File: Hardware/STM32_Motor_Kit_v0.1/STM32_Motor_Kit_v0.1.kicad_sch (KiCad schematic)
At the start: 13 parts

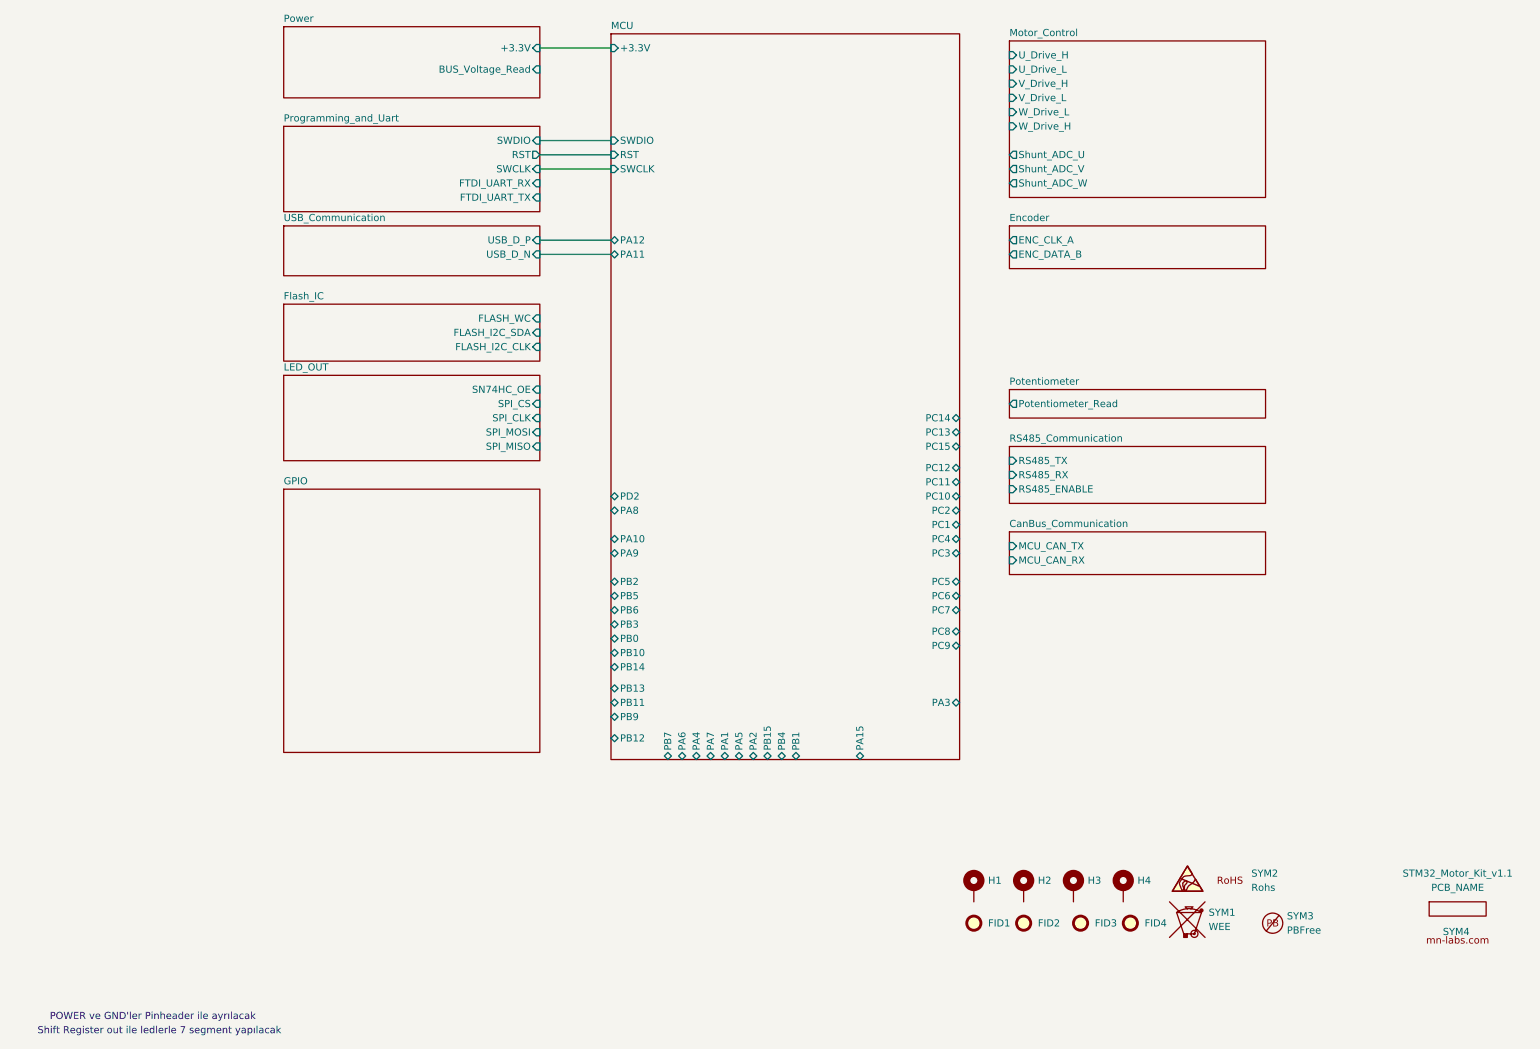
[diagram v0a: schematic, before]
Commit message: Firmware Configuration added, Motor Control Pins and BackEMF Analog Pins setted.
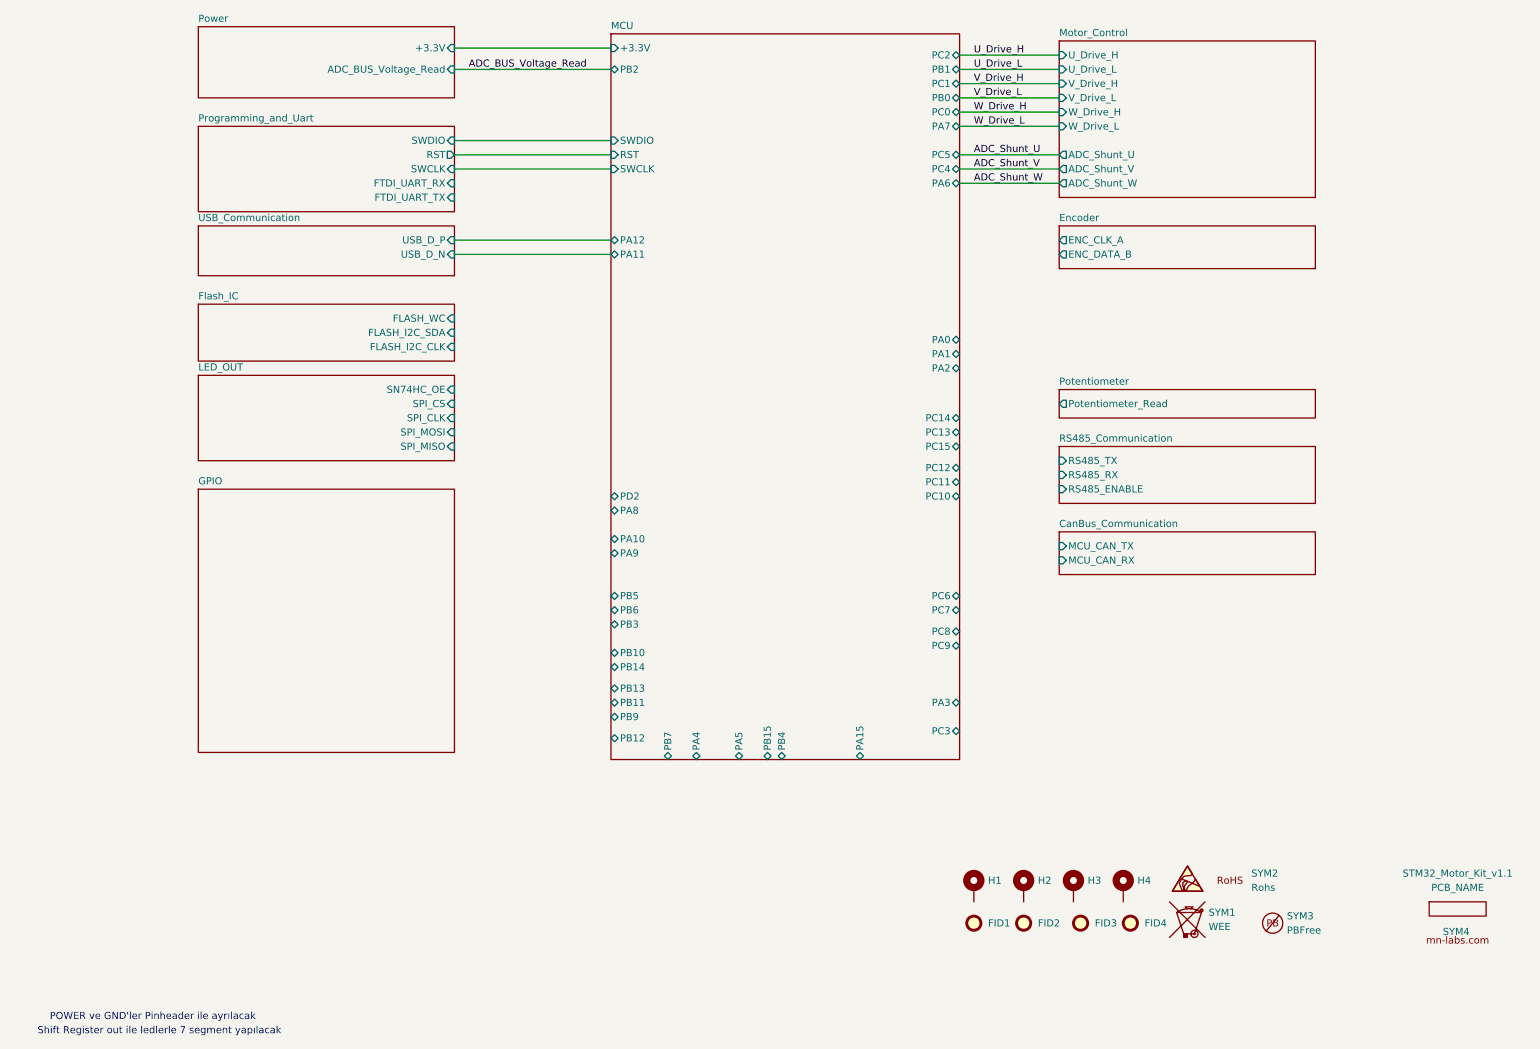
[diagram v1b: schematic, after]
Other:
- sheet MCU ports: added PA0, PC0; removed none
- sheet Motor_Control ports: added ADC_Shunt_U, ADC_Shunt_V, ADC_Shunt_W; removed Shunt_ADC_U, Shunt_ADC_V, Shunt_ADC_W
- sheet Power ports: added ADC_BUS_Voltage_Read; removed BUS_Voltage_Read

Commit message: 22.08.2024
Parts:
- added R104, R105, R106, R107, R108, R109, R110, R111, R112, R113, R114, R115, R116, R85, R86: 33R, AKE_Resistor_SMD:RES_0603, symbol AKE_Resistor:Resistor_US
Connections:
- net MCU/PA0: now also R111.1
- net MCU/PA1: now also R112.1
- net MCU/PA4: now also R110.1
- net MCU/PA5: now also R109.1
- net MCU/PB11: now also R113.1
- net MCU/PB12: now also R105.1
- net MCU/PB13: now also R85.1
- net MCU/PB14: now also R86.1
- net MCU/PB15: now also R104.1
- net MCU/PC10: now also R107.1
- net MCU/PC11: now also R106.1
- net MCU/PC12: now also R108.1
- net MCU/PC14: now also R115.1
- net MCU/PC15: now also R116.1
- net MCU/PC6: now also R114.1
- new net GPIO/Pin_1: R85.2
- new net GPIO/Pin_10: R111.2
- new net GPIO/Pin_11: R112.2
- new net GPIO/Pin_12: R113.2
- new net GPIO/Pin_13: R114.2
- new net GPIO/Pin_14: R115.2
- new net GPIO/Pin_15: R116.2
- new net GPIO/Pin_2: R86.2
- new net GPIO/Pin_3: R104.2
- new net GPIO/Pin_4: R105.2
- new net GPIO/Pin_5: R106.2
- new net GPIO/Pin_6: R107.2
- new net GPIO/Pin_7: R108.2
- new net GPIO/Pin_8: R109.2
- new net GPIO/Pin_9: R110.2
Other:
- added sheet User_Command (User_Command.kicad_sch)
- sheet GPIO ports: added Pin_1, Pin_10, Pin_11, Pin_12, Pin_13, Pin_14, Pin_15, Pin_2, Pin_3, Pin_4, Pin_5, Pin_6, Pin_7, Pin_8, Pin_9; removed none
- sheet MCU ports: added PB8; removed none

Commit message: 23.08.2024
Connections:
- net GPIO/Pin_1: now also R108.2; no longer R85.2
- net GPIO/Pin_10: now also R114.2; no longer R111.2
- net GPIO/Pin_11: now also R105.2; no longer R112.2
- net GPIO/Pin_13: now also R104.2; no longer R114.2
- net GPIO/Pin_14: now also R86.2; no longer R115.2
- net GPIO/Pin_15: now also R85.2; no longer R116.2
- net GPIO/Pin_2: now also R106.2; no longer R86.2
- net GPIO/Pin_3: now also R107.2; no longer R104.2
- net GPIO/Pin_4: now also R115.2; no longer R105.2
- net GPIO/Pin_5: now also R116.2; no longer R106.2
- net GPIO/Pin_6: now also R111.2; no longer R107.2
- net GPIO/Pin_7: now also R112.2; no longer R108.2
- net GPIO/Pin_8: now also R110.2; no longer R109.2
- net GPIO/Pin_9: now also R109.2; no longer R110.2
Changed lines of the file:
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@@
 		)
 		(pin "Pin_10" input
-			(at 87.63 127 0)
+			(at 87.63 134.62 0)
 			(effects
 				(font
@@
 		)
 		(pin "Pin_14" input
-			(at 87.63 137.16 0)
+			(at 87.63 104.14 0)
 			(effects
 				(font
@@
 		)
 		(pin "Pin_1" input
+			(at 87.63 118.11 0)
+			(effects
+				(font
+					(size 1.27 1.27)
+				)
+				(justify right)
+			)
+		)
+		(pin "Pin_3" input
+			(at 87.63 115.57 0)
+			(effects
+				(font
+					(size 1.27 1.27)
+				)
+				(justify right)
+			)
+		)
+		(pin "Pin_5" input
+			(at 87.63 139.7 0)
+			(effects
+				(font
+					(size 1.27 1.27)
+				)
+				(justify right)
+			)
+		)
+		(pin "Pin_7" input
+			(at 87.63 129.54 0)
+			(effects
+				(font
+					(size 1.27 1.27)
+				)
+				(justify right)
+			)
+		)
+		(pin "Pin_13" input
+			(at 87.63 106.68 0)
+			(effects
+				(font
+					(size 1.27 1.27)
+				)
+				(justify right)
+			)
+		)
+		(pin "Pin_15" input
 			(at 87.63 101.6 0)
 			(effects
@@
 			)
 		)
-		(pin "Pin_3" input
-			(at 87.63 106.68 0)
+		(pin "Pin_9" input
+			(at 87.63 121.92 0)
 			(effects
 				(font
@@
 			)
 		)
-		(pin "Pin_5" input
+		(pin "Pin_11" input
+			(at 87.63 109.22 0)
+			(effects
+				(font
+					(size 1.27 1.27)
+				)
+				(justify right)
+			)
+		)
+		(pin "Pin_8" input
+			(at 87.63 124.46 0)
+			(effects
+				(font
+					(size 1.27 1.27)
+				)
+				(justify right)
+			)
+		)
+		(pin "Pin_4" input
+			(at 87.63 137.16 0)
+			(effects
+				(font
+					(size 1.27 1.27)
+				)
+				(justify right)
+			)
+		)
+		(pin "Pin_2" input
 			(at 87.63 113.03 0)
 			(effects
@@
 			)
 		)
-		(pin "Pin_7" input
-			(at 87.63 118.11 0)
+		(pin "Pin_6" input
+			(at 87.63 127 0)
 			(effects
 				(font
-					(size 1.27 1.27)
-				)
-				(justify right)
-			)
-		)
-		(pin "Pin_13" input
-			(at 87.63 134.62 0)
-			(effects
-				(font
-					(size 1.27 1.27)
-				)
-				(justify right)
-			)
-		)
-		(pin "Pin_15" input
-			(at 87.63 139.7 0)
-			(effects
-				(font
-					(size 1.27 1.27)
-				)
-				(justify right)
-			)
-		)
-		(pin "Pin_9" input
-			(at 87.63 124.46 0)
-			(effects
-				(font
-					(size 1.27 1.27)
-				)
-				(justify right)
-			)
-		)
-		(pin "Pin_11" input
-			(at 87.63 129.54 0)
-			(effects
-				(font
-					(size 1.27 1.27)
-				)
-				(justify right)
-			)
-		)
-		(pin "Pin_8" input
-			(at 87.63 121.92 0)
-			(effects
-				(font
-					(size 1.27 1.27)
-				)
-				(justify right)
-			)
-		)
-		(pin "Pin_4" input
-			(at 87.63 109.22 0)
-			(effects
-				(font
-					(size 1.27 1.27)
-				)
-				(justify right)
-			)
-		)
-		(pin "Pin_2" input
-			(at 87.63 104.14 0)
-			(effects
-				(font
-					(size 1.27 1.27)
-				)
-				(justify right)
-			)
-		)
-		(pin "Pin_6" input
-			(at 87.63 115.57 0)
-			(effects
-				(font

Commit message: 26.08.2024
1nF 2KV chassis ile GND arasına ekledim. PCB'de güncellemeler oldu.
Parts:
- added C115, C74: 1nF_2KV, AKE_Capacitor_SMD:CAP_1206, symbol AKE_Capacitor:Capacitor_UnPolarised
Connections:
- net GPIO/Pin_11: now also R104.2; no longer R105.2
- net GPIO/Pin_12: now also R105.2; no longer R113.2
- net GPIO/Pin_13: now also R85.2; no longer R104.2
- net GPIO/Pin_15: now also R113.2; no longer R85.2
- net MCU/PB12: now also R86.1; no longer R105.1
- net MCU/PB14: now also R105.1; no longer R86.1
- net Chassis: now reaches H4.1
- net Chassis: now also H1.1, H2.1, H3.1, C115.1, C74.1
- new net GND: C115.2, C74.2
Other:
- moved on the sheet: H1, H2, H3, H4, R105, R86

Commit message: 29.08.2024
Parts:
- removed STM32_Motor_Kit_v1.1: PCB_NAME, AKE_Logo:PCB_NAME, symbol AKE_Symbol:PCB_NAME
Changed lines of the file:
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@@
-	)
-	(symbol
-		(lib_id "AKE_Symbol:PCB_NAME")
-		(at 266.7 173.99 0)
-		(unit 1)
-		(exclude_from_sim no)
-		(in_bom yes)
-		(on_board yes)
-		(dnp no)
-		(fields_autoplaced yes)
-		(property "Reference" "STM32_Motor_Kit_v1.1"
-			(at 266.7 167.64 0)
-			(effects
-				(font
-					(size 1.27 1.27)
-				)
-			)
-		)
-		(property "Value" "PCB_NAME"
-			(at 266.7 170.18 0)
-			(effects
-				(font
-					(size 1.27 1.27)
-				)
-			)
-		)
-		(property "Footprint" "AKE_Logo:PCB_NAME"
-			(at 265.43 176.53 0)
-			(effects
-				(font
-					(size 1.27 1.27)
-				)
-				(hide yes)
-			)
-		)
-		(property "Datasheet" ""
-			(at 266.7 173.99 0)
-			(effects
-				(font
-					(size 1.27 1.27)
-				)
-				(hide yes)
-			)
-		)
-		(property "Description" ""
-			(at 266.7 173.99 0)
-			(effects
-				(font
-					(size 1.27 1.27)
-				)
-				(hide yes)
-			)
-		)
-		(instances
-			(project "STM32_Motor_Kit_v0.1"
-				(path "/350b6aea-94d6-460b-86d9-ade6c51fbb19"
-					(reference "STM32_Motor_Kit_v1.1")
-					(unit 1)
-				)
-			)
-		)
 	)
 	(symbol

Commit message: 01.09.2024
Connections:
- net GPIO/Pin_1 renamed PC12
- net GPIO/Pin_10 renamed PC6
- net GPIO/Pin_11 renamed PB15
- net GPIO/Pin_12 renamed PB14
- net GPIO/Pin_13 renamed PB13
- net GPIO/Pin_14 renamed PB12
- net GPIO/Pin_15 renamed PB11
- net GPIO/Pin_2 renamed PC11
- net GPIO/Pin_3 renamed PC10
- net GPIO/Pin_4 renamed PC14
- net GPIO/Pin_5 renamed PC15
- net GPIO/Pin_6 renamed PA0
- net GPIO/Pin_7 renamed PA1
- net GPIO/Pin_8 renamed PA4
- net GPIO/Pin_9 renamed PA5
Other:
- moved on the sheet: R104, R105, R106, R107, R108, R109, R110, R111, R112, R113, R114, R115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

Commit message: Şemada güncellemeler yaptım, PCB'de revizyon yapılacak
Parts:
- H1, H2, H3, H4, SYM1, SYM2, SYM3, SYM4: now not fitted
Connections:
- net MCU/PA0 renamed MCU/PB7
- net MCU/PA1: no longer names the net of R112.1
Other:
- sheet Encoder ports: added ENC_CH1, ENC_CH2, ENC_CH3; removed ENC_CLK_A, ENC_DATA_B
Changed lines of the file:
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@@
 	(wire
 		(pts
+			(xy 177.8 59.69) (xy 203.2 59.69)
+		)
+		(stroke
+			(width 0)
+			(type default)
+		)
+	)
+	(wire
+		(pts
 			(xy 107.95 113.03) (xy 115.57 113.03)
 		)
@@
 		)
 	)
+	(label "ENC_CH2"
+		(at 182.88 57.15 0)
+		(fields_autoplaced yes)
+		(effects
+			(font
+				(size 1.27 1.27)
+			)
+			(justify left bottom)
+		)
+	)
 	(label "PC14"
 		(at 90.17 137.16 0)
@@
 		)
 	)
-	(label "RS485_ENABLE"
-		(at 179.07 99.06 0)
+	(label "ENC_CH1"
+		(at 182.88 54.61 0)
 		(fields_autoplaced yes)
 		(effects
@@
 		)
 	)
-	(label "RST"
-		(at 90.17 39.37 0)
+	(label "RS485_ENABLE"
+		(at 179.07 99.06 0)
 		(fields_autoplaced yes)
 		(effects
@@
 		)
 	)
-	(label "V_Drive_L"
-		(at 181.61 29.21 0)
+	(label "RST"
+		(at 90.17 39.37 0)
 		(fields_autoplaced yes)
 		(effects
@@
 		)
 	)
-	(label "ADC_BUS_Voltage_Read"
-		(at 90.17 24.13 0)
+	(label "V_Drive_L"
+		(at 181.61 29.21 0)
 		(fields_autoplaced yes)
 		(effects
@@
 		)
 	)
-	(label "ENC_CLK_A"
-		(at 181.61 54.61 0)
+	(label "ADC_BUS_Voltage_Read"
+		(at 90.17 24.13 0)
 		(fields_autoplaced yes)
 		(effects
@@
 		)
 	)
-	(label "PB14"
-		(at 90.17 104.14 0)
+	(label "ENC_CH3"
+		(at 182.88 59.69 0)
 		(fields_autoplaced yes)
 		(effects
@@
 		)
 	)
-	(label "PA1"
-		(at 90.17 129.54 0)
+	(label "PB14"
+		(at 90.17 104.14 0)
 		(fields_autoplaced yes)
 		(effects
@@
 		)
 	)
-	(label "ENC_DATA_B"
-		(at 181.61 57.15 0)
+	(label "PA1"
+		(at 90.17 129.54 0)
 		(fields_autoplaced yes)
 		(effects
@@
 		(in_bom no)
 		(on_board no)
-		(dnp no)
+		(dnp yes)
 		(fields_autoplaced yes)
 		(property "Reference" "#SYM1"
@@
 		(in_bom yes)
 		(on_board yes)
-		(dnp no)
+		(dnp yes)
 		(fields_autoplaced yes)
 		(property "Reference" "SYM1"
@@
 		(in_bom yes)
 		(on_board yes)
-		(dnp no)
+		(dnp yes)
 		(fields_autoplaced yes)
 		(property "Reference" "H4"
@@
 		(in_bom yes)
 		(on_board yes)
-		(dnp no)
+		(dnp yes)
 		(fields_autoplaced yes)
 		(property "Reference" "H2"
@@
 		(in_bom yes)
 		(on_board yes)
-		(dnp no)
+		(dnp yes)
 		(fields_autoplaced yes)
 		(property "Reference" "H1"
@@
 		(in_bom yes)
 		(on_board yes)
-		(dnp no)
+		(dnp yes)
 		(fields_autoplaced yes)
 		(property "Reference" "SYM3"
@@
 		(in_bom no)
 		(on_board no)
-		(dnp no)
+		(dnp yes)
 		(property "Reference" "SYM4"
 			(at 266.446 178.054 0)
@@
 		(in_bom yes)
 		(on_board yes)
-		(dnp no)
+		(dnp yes)
 		(fields_autoplaced yes)
 		(property "Reference" "H3"
@@
 		(in_bom yes)
 		(on_board yes)
-		(dnp no)
+		(dnp yes)
 		(fields_autoplaced yes)
 		(property "Reference" "SYM2"
@@
 	(sheet
 		(at 203.2 52.07)
-		(size 45.72 7.62)
+		(size 45.72 10.16)
 		(fields_autoplaced yes)
 		(stroke
@@
 		)
 		(property "Sheetfile" "Encoder.kicad_sch"
-			(at 203.2 60.2746 0)
+			(at 203.2 62.8146 0)
 			(effects
 				(font
@@
 			)
 		)
-		(pin "ENC_DATA_B" output
+		(pin "ENC_CH2" output
 			(at 203.2 57.15 180)
 			(effects
@@
 			)
 		)
-		(pin "ENC_CLK_A" output
+		(pin "ENC_CH1" output
 			(at 203.2 54.61 180)
 			(effects
@@
 			)
 		)
+		(pin "ENC_CH3" output
+			(at 203.2 59.69 180)
+			(effects
+				(font
+					(size 1.27 1.27)
+				)
+				(justify left)
+			)
+		)
 		(instances
 			(project "STM32_Motor_Kit_v0.1"
@@
 		)
 		(pin "PB6" bidirectional
-			(at 177.8 54.61 0)
+			(at 177.8 99.06 0)
 			(effects
 				(font
@@
 		)
 		(pin "PB10" bidirectional
-			(at 177.8 99.06 0)
+			(at 177.8 59.69 0)
 			(effects
 				(font
@@
 		)
 		(pin "PA1" bidirectional
-			(at 115.57 129.54 180)
+			(at 177.8 57.15 0)
 			(effects
 				(font
 					(size 1.27 1.27)
 				)
-				(justify left)
+				(justify right)
 			)
 		)
@@
 		)
 		(pin "PB7" bidirectional
-			(at 177.8 57.15 0)
+			(at 115.57 127 180)
 			(effects
 				(font
 					(size 1.27 1.27)
 				)
-				(justify right)
+				(justify left)
 			)
 		)
@@
 		)
 		(pin "PA0" bidirectional
-			(at 115.57 127 180)
+			(at 177.8 54.61 0)
 			(effects
 				(font
 					(size 1.27 1.27)
 				)
-				(justify left)
+				(justify right)
 			)
 		)

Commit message: 16.09.2024
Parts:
- removed R112: 33R, AKE_Resistor_SMD:RES_0603, symbol AKE_Resistor:Resistor_US
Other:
- sheet GPIO ports: added none; removed Pin_7
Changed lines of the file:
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@@
 	(wire
 		(pts
-			(xy 107.95 129.54) (xy 115.57 129.54)
-		)
-		(stroke
-			(width 0)
-			(type default)
-		)
-	)
-	(wire
-		(pts
 			(xy 107.95 106.68) (xy 115.57 106.68)
 		)
@@
 	(wire
 		(pts
-			(xy 87.63 129.54) (xy 102.87 129.54)
-		)
-		(stroke
-			(width 0)
-			(type default)
-		)
-	)
-	(wire
-		(pts
 			(xy 107.95 127) (xy 115.57 127)
 		)
@@
 		)
 	)
-	(label "PA1"
-		(at 90.17 129.54 0)
-		(fields_autoplaced yes)
-		(effects
-			(font
-				(size 1.27 1.27)
-			)
-			(justify left bottom)
-		)
-	)
 	(label "SWCLK"
 		(at 90.17 41.91 0)
@@
 	(symbol
 		(lib_id "AKE_Resistor:Resistor_US")
-		(at 105.41 129.54 270)
-		(unit 1)
-		(exclude_from_sim no)
-		(in_bom yes)
-		(on_board yes)
-		(dnp no)
-		(property "Reference" "R112"
-			(at 108.458 128.524 90)
-			(effects
-				(font
-					(size 1.27 1.27)
-				)
-			)
-		)
-		(property "Value" "33R"
-			(at 101.854 128.524 90)
-			(effects
-				(font
-					(size 1.27 1.27)
-				)
-			)
-		)
-		(property "Footprint" "AKE_Resistor_SMD:RES_0603"
-			(at 105.41 129.54 0)
-			(effects
-				(font
-					(size 1.27 1.27)
-				)
-				(hide yes)
-			)
-		)
-		(property "Datasheet" "~"
-			(at 105.41 129.54 0)
-			(effects
-				(font
-					(size 1.27 1.27)
-				)
-				(hide yes)
-			)
-		)
-		(property "Description" ""
-			(at 105.41 129.54 0)
-			(effects
-				(font
-					(size 1.27 1.27)
-				)
-				(hide yes)
-			)
-		)
-		(property "MFG P/N" "*"
-			(at 107.95 133.35 0)
-			(effects
-				(font
-					(size 1.27 1.27)
-				)
-				(hide yes)
-			)
-		)
-		(pin "1"
-		)
-		(pin "2"
-		)
-		(instances
-			(project "STM32_Motor_Kit_v0.1"
-				(path "/350b6aea-94d6-460b-86d9-ade6c51fbb19"
-					(reference "R112")
-					(unit 1)
-				)
-			)
-		)
-	)
-	(symbol
-		(lib_id "AKE_Resistor:Resistor_US")
 		(at 105.41 134.62 270)
 		(unit 1)
@@
 			(effects
 				(font
-					(size 1.27 1.27)
-				)
-				(justify right)
-			)
-		)
-		(pin "Pin_7" input
-			(at 87.63 129.54 0)
-			(effects
-				(font
